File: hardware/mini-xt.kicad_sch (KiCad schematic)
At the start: 0 parts

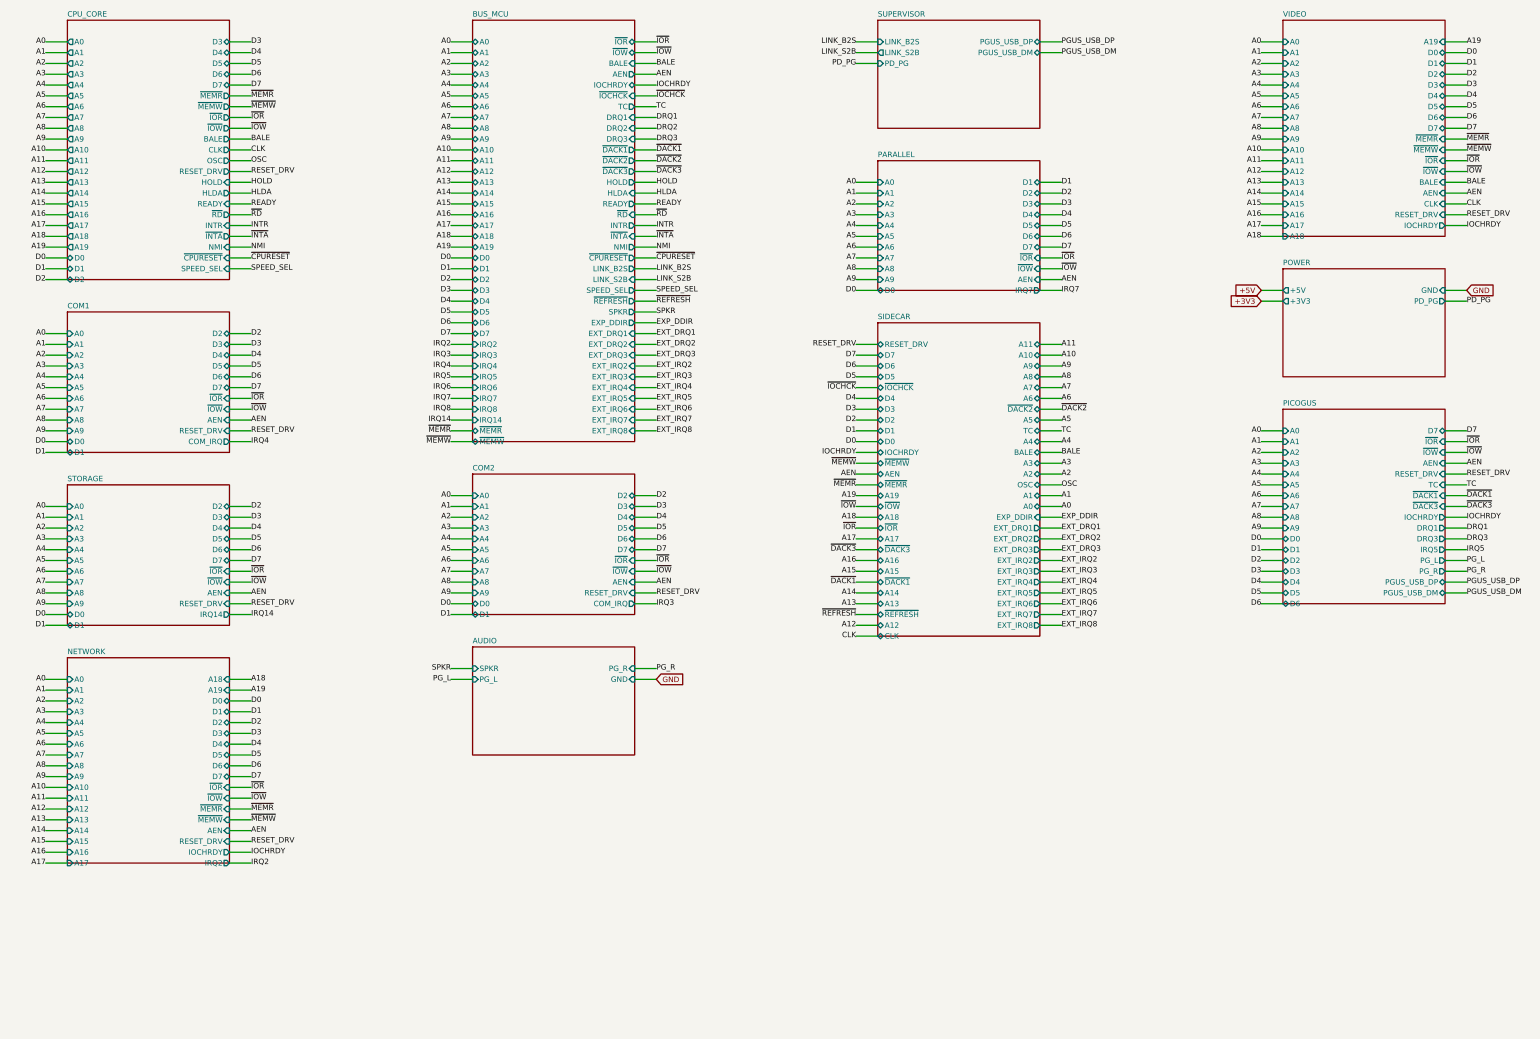
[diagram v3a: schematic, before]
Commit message: com_port: merge COM1+COM2 onto one sheet with shared decode/IRQ glue
One address decoder serves both ports (0x3F8/0x2F8 differ only in A8:
common A3-A7,A9,~AEN term ANDed with A8/~A8) and one 74LVC125A gates
both IRQs -- glue drops from 8 chips to 4, COM subsystem 12 ICs -> 8
(56 comps -> 41). Base addresses hardwired (J2 straps existed only
because one generic sheet was instanced at both addresses); console
header + RX select drawn once on COM1; enables now JP3/JP4; interface
exposes IRQ4/IRQ3 directly instead of the COM_IRQ remap. Sheet moves
to A2 paper; validate_sheet.py now honors PAPER. Docs/notes aligned.

Co-Authored-By: Claude Fable 5 <noreply@anthropic.com>
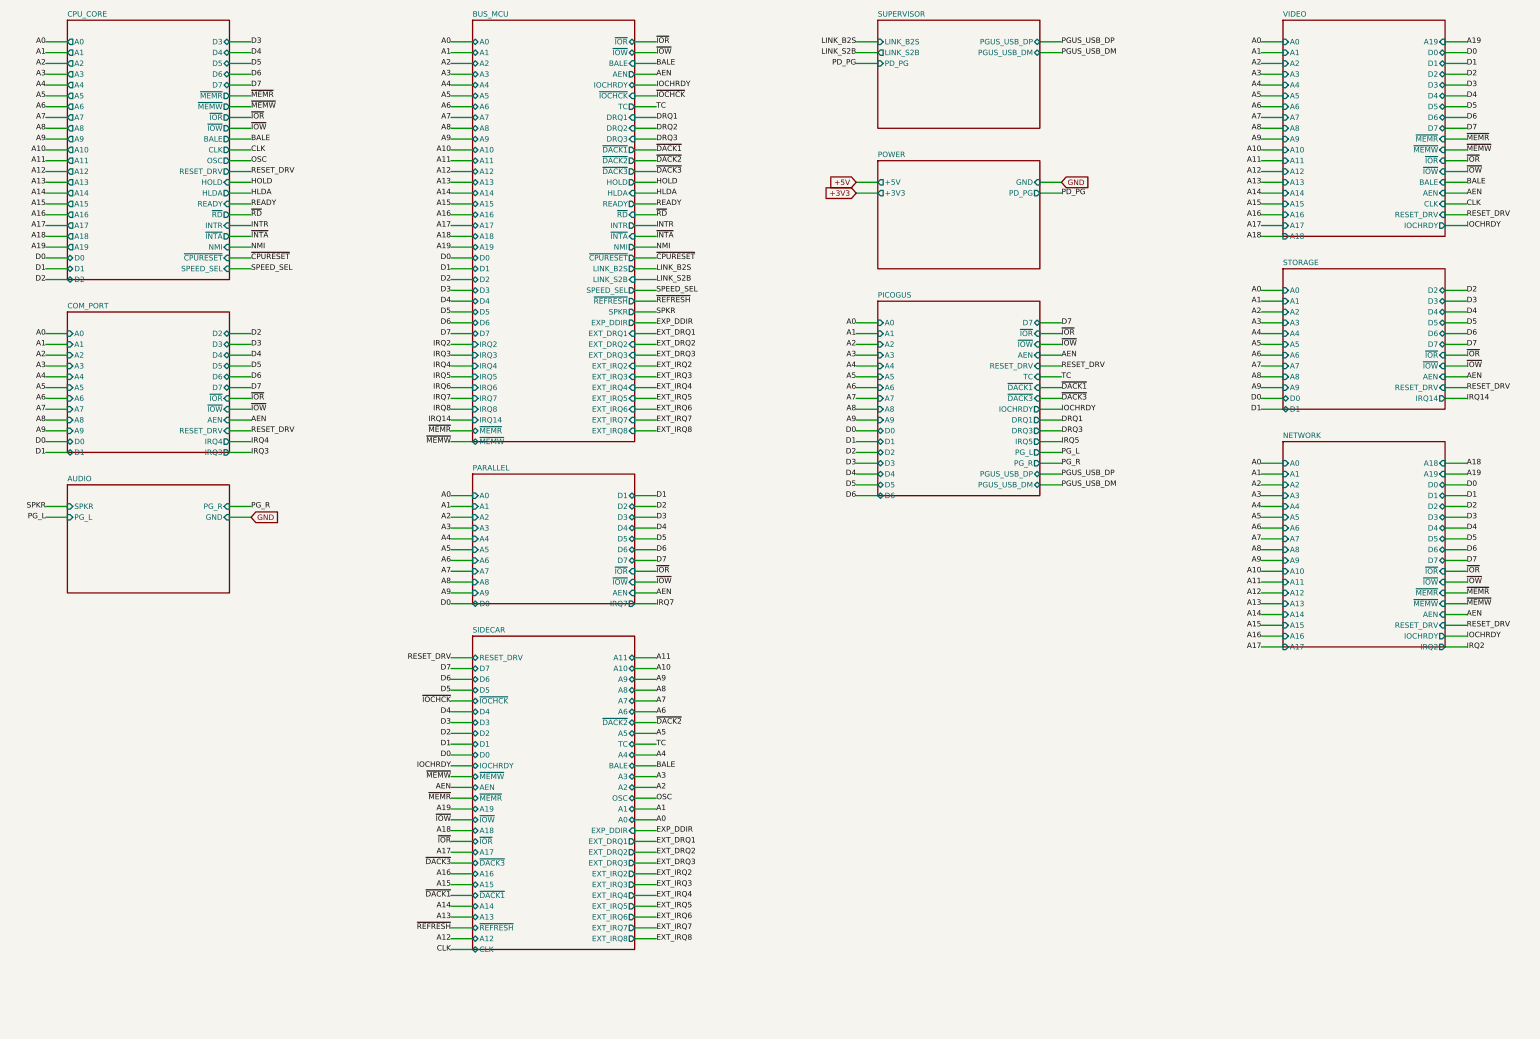
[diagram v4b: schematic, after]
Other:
- sheet COM1 renamed COM_PORT
- removed sheet COM2
- sheet COM_PORT ports: added IRQ3, IRQ4; removed COM_IRQ
